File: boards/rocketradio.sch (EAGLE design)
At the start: 6 parts, among them X1 BU-SMA-H

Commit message: moving to new repo
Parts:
- added U$2: ATTINY85SOCKET, evan:ATTINY85SOCKET
- added U$3, U$4, U$5, U$6, U$7, U$8, U$9: 1N4148W, evan:1N4148W
- U$1: value (none) -> DRA818V; device dorji:DORJI -> dorji:DORJIDRA818V
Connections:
- new net N$10: U$1.AF_OUT
- new net N$11: U$1.RXD, U$6.A
- new net N$12: U$8.C, U$9.A
- new net N$13: U$7.C, U$8.A
- new net N$14: U$2.PB0(PCINT0/MOSI/AIN0), U$7.A
- new net N$15: U$6.C
- new net N$16: U$3.A
- new net N$6: U$1.TXD, U$4.C
- new net N$7: U$4.A, U$5.C
- new net N$8: U$3.C, U$5.A
- new net N$9: U$1.MIC_IN
- net +3V3: now also R2.1
- net GND: no longer R2.1
- net N$4: now also U$9.C
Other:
- note added: "to mod"
- moved on the sheet: R1, R2

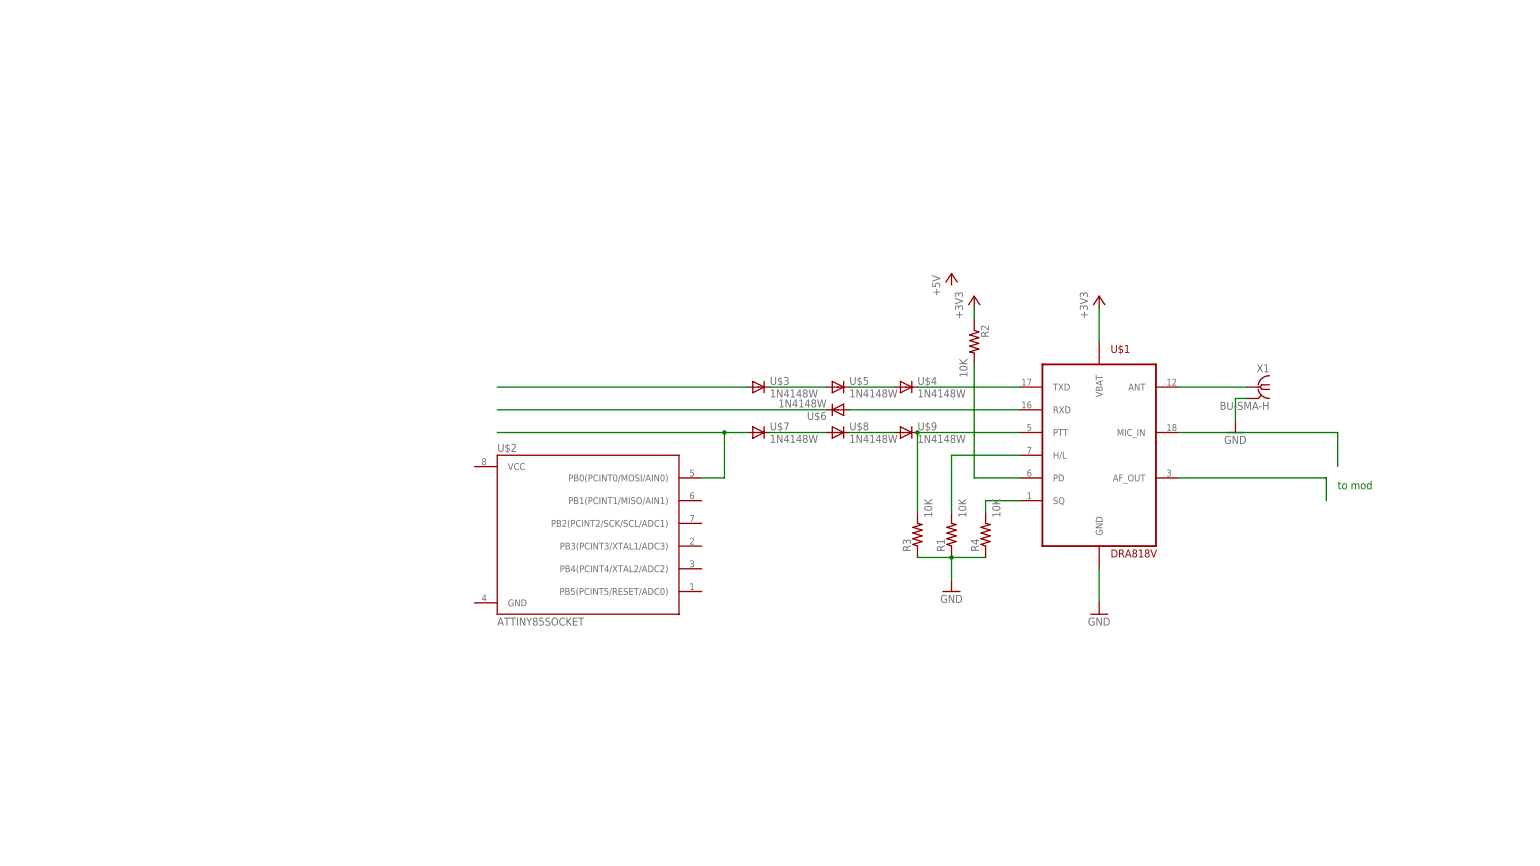
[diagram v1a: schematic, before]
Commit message: update board with correct modem pinout
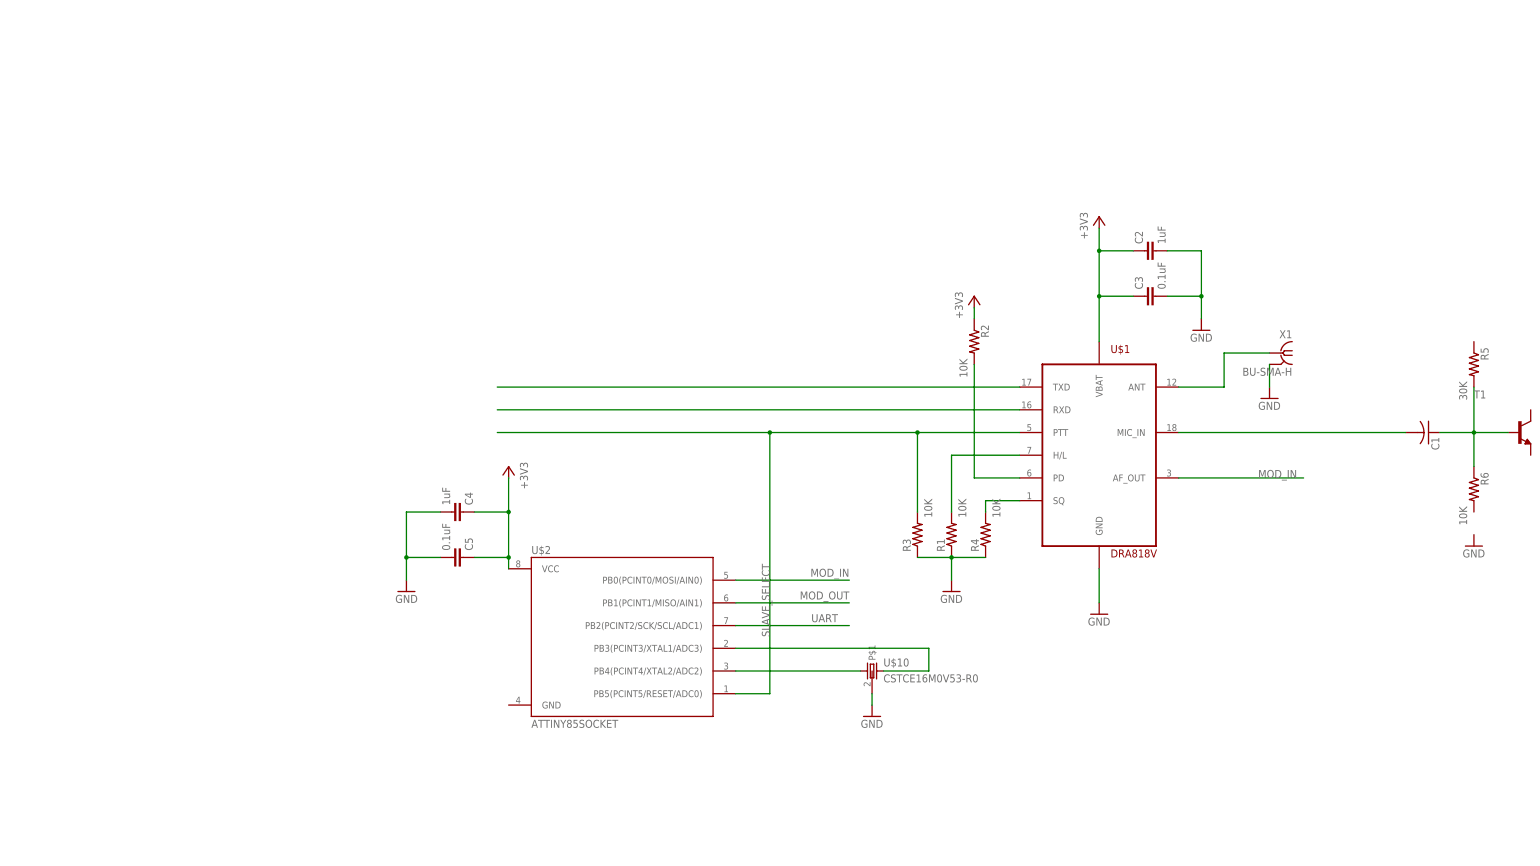
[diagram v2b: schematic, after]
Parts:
- removed U$3, U$4, U$5, U$6, U$7, U$8, U$9: 1N4148W, evan:1N4148W
- added C1: (no value), rcl:C-USC0603
- added C2, C4: 1uF, rcl:C-EUC0603
- added C3, C5: 0.1uF, rcl:C-EUC0603
- added R5: 30K, rcl:R-US_R0603
- added R6: 10K, rcl:R-US_R0603
- added T1: (no value), transistor:MMBT2222ALT1-NPN-SOT23-BEC
- added U$10: CSTCE16M0V53-R0, evan:CSTCE16M0V53-R0
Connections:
- removed net N$10: U$1.AF_OUT
- removed net N$11: U$1.RXD, U$6.A
- removed net N$12: U$8.C, U$9.A
- removed net N$13: U$7.C, U$8.A
- removed net N$14: U$2.PB0(PCINT0/MOSI/AIN0), U$7.A
- removed net N$4: R3.2, U$1.PTT, U$9.C
- removed net N$6: U$1.TXD, U$4.C
- removed net N$7: U$4.A, U$5.C
- removed net N$8: U$3.C, U$5.A
- new net MOD_IN: U$1.AF_OUT, U$2.PB0(PCINT0/MOSI/AIN0)
- new net MOD_OUT: U$2.PB1(PCINT1/MISO/AIN1)
- new net N$17: U$10.2, U$2.PB3(PCINT3/XTAL1/ADC3)
- new net N$18: U$10.1, U$2.PB4(PCINT4/XTAL2/ADC2)
- new net N$20: C1.1, R5.2, R6.1, T1.B
- new net SLAVE_SELECT: R3.2, U$1.PTT, U$2.PB5(PCINT5/RESET/ADC0)
- new net UART: U$2.PB2(PCINT2/SCK/SCL/ADC1)
- net +3V3: now also C2.1, C3.1, C4.1, C5.1, U$2.VCC
- net GND: now also C2.2, C3.2, C4.2, C5.2, U$10.P$1
- net N$15: now also U$1.RXD; no longer U$6.C
- net N$16: now also U$1.TXD; no longer U$3.A
- net N$9: now also C1.2
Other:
- note removed: "to mod"
- moved on the sheet: U$2, X1

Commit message: add micro
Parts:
- added C10, C7, C8, C9: 0.1uF, rcl:C-EUC0603
- added C6: 1uF, rcl:C-EUC0603
- added R10, R11, R12, R7, R8, R9: (no value), rcl:R-US_R0603
- added U$3: ATTINY85SOCKET, evan:ATTINY85SOCKET
- C1: value (none) -> 0.1uF; device rcl:C-USC0603 -> rcl:C-EUC0603
- R5: value 30K -> (none)
- R6: value 10K -> (none)
- T1: value (none) -> 2N2222; device transistor:MMBT2222ALT1-NPN-SOT23-BEC -> transistor:2N2222
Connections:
- removed net N$15: U$1.RXD
- removed net N$16: U$1.TXD
- removed net N$20: C1.1, R5.2, R6.1, T1.B
- removed net N$9: C1.2, U$1.MIC_IN
- new net MIC_IN: C8.1, U$1.MIC_IN
- new net N$10: C9.1, R9.2, T1.E
- new net N$11: C10.1, R10.1, T1.C
- new net N$6: C8.2, R7.2, R8.1
- new net N$7: C1.1, R5.1, R6.2, T1.B
- new net N$8: C1.2, U$1.AF_OUT
- new net RADIO_CONTROL: U$1.RXD, U$3.PB3(PCINT3/XTAL1/ADC3)
- net +3V3: now also C6.1, C7.1, R1.1, R10.2, R11.2, R3.1, R5.2, U$3.VCC
- net GND: now also C6.2, C7.2, C9.2, R12.1, R6.1, R8.2, R9.1, U$2.GND, U$3.GND; no longer R1.1, R3.1
- net MOD_IN: now also C10.2, R11.1, R12.2; no longer U$1.AF_OUT
- net MOD_OUT: now also R7.1
- net SLAVE_SELECT: now also U$3.PB5(PCINT5/RESET/ADC0)
- net UART: now also U$3.PB2(PCINT2/SCK/SCL/ADC1)
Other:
- note added: "MAIN MICRO"
- note added: "MODEM"
- note added: "RADIO"
- moved on the sheet: C1, C2, C3, C4, C5, R1, R2, R3, R4, R5, R6, T1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

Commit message: finish dumb node, update sims
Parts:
- removed C10: 0.1uF, rcl:C-EUC0603
- removed R10, R11, R12, R8, R9: (no value), rcl:R-US_R0603
- removed U$10: CSTCE16M0V53-R0, evan:CSTCE16M0V53-R0
- removed U$2: ATTINY85SOCKET, evan:ATTINY85SOCKET
- added BATT+, BATT-, COM, JP1, JP3, NC, NO: (no value), evan:PINHD-1X1
- added K1: G5LE, relay:G5LE
- added MODEM: ATTINY85SOCKET, evan:ATTINY85SOCKET
- C1: value 0.1uF -> 10uF; device rcl:C-EUC0603 -> rcl:C-US025-050X050
- C4, C6: value 1uF -> 0.1uF
- C5, C7: value 0.1uF -> 1uF
- R5, R6, R7: value (none) -> 400
- renumbered U$3 to MICRO
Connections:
- removed net N$17: U$10.2, U$2.PB3(PCINT3/XTAL1/ADC3)
- removed net N$18: U$10.1, U$2.PB4(PCINT4/XTAL2/ADC2)
- removed net N$8: C1.2, U$1.AF_OUT
- removed net SLAVE_SELECT: MICRO.PB5(PCINT5/RESET/ADC0), R3.2, U$1.PTT, U$2.PB5(PCINT5/RESET/ADC0)
- removed net UART: MICRO.PB2(PCINT2/SCK/SCL/ADC1), U$2.PB2(PCINT2/SCK/SCL/ADC1)
- new net DATA_IN: MICRO.PB2(PCINT2/SCK/SCL/ADC1), MODEM.PB3(PCINT3/XTAL1/ADC3)
- new net DATA_OUT: MICRO.PB1(PCINT1/MISO/AIN1), MODEM.PB4(PCINT4/XTAL2/ADC2)
- new net MOD_SELECT: MICRO.PB5(PCINT5/RESET/ADC0), MODEM.PB5(PCINT5/RESET/ADC0), R3.2, U$1.PTT
- new net N$4: R5.2, U$1.AF_OUT
- new net N$9: K12.S, NO.1
- new net TRIGGER: MICRO.PB0(PCINT0/MOSI/AIN0), R7.2
- net +3V3: now also BATT+.1, C1.1, JP1.1, K11.1, MODEM.VCC; no longer R10.2, R11.2, R5.2, U$2.VCC
- net GND: now also BATT-.1, C1.2, C8.1, C9.1, JP3.1, MODEM.GND, T1.E; no longer C9.2, R12.1, R6.1, R8.2, R9.1, U$10.P$1, U$2.GND
- net MIC_IN: now also C9.2, R6.1; no longer C8.1
- net MOD_IN: now also C8.2, MODEM.PB2(PCINT2/SCK/SCL/ADC1), R5.1; no longer C10.2, R11.1, R12.2, U$2.PB0(PCINT0/MOSI/AIN0)
- net MOD_OUT: now also MODEM.PB1(PCINT1/MISO/AIN1), R6.2; no longer R7.1, U$2.PB1(PCINT1/MISO/AIN1)
- net N$10: now also K12.O, NC.1; no longer C9.1, R9.2, T1.E
- net N$11: now also COM.1, K12.P; no longer C10.1, R10.1, T1.C
- net N$6: now also R7.1, T1.B; no longer C8.2, R7.2, R8.1
- net N$7: now also K11.2, T1.C; no longer C1.1, R5.1, R6.2, T1.B
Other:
- note added: "BATT"
- note removed: "MAIN MICRO"
- note removed: "MODEM"
- moved on the sheet: C1, C2, C3, C4, C5, C6, C7, C8, C9, R5, R6, R7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
